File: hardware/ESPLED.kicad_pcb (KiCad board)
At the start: 2 copper layers, 100 x 50 mm, 52 parts, among them CON1 BARREL_JACK, J1 USB, J2 LED_CON_RGB, J3 LED_CON_WW, J4 MIC, P1 LED_CON_SCREW, P2 LED_CON_SCREW, P3 LED_CON_SCREW, Q1 IRLZ34N, Q2 IRLZ34N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

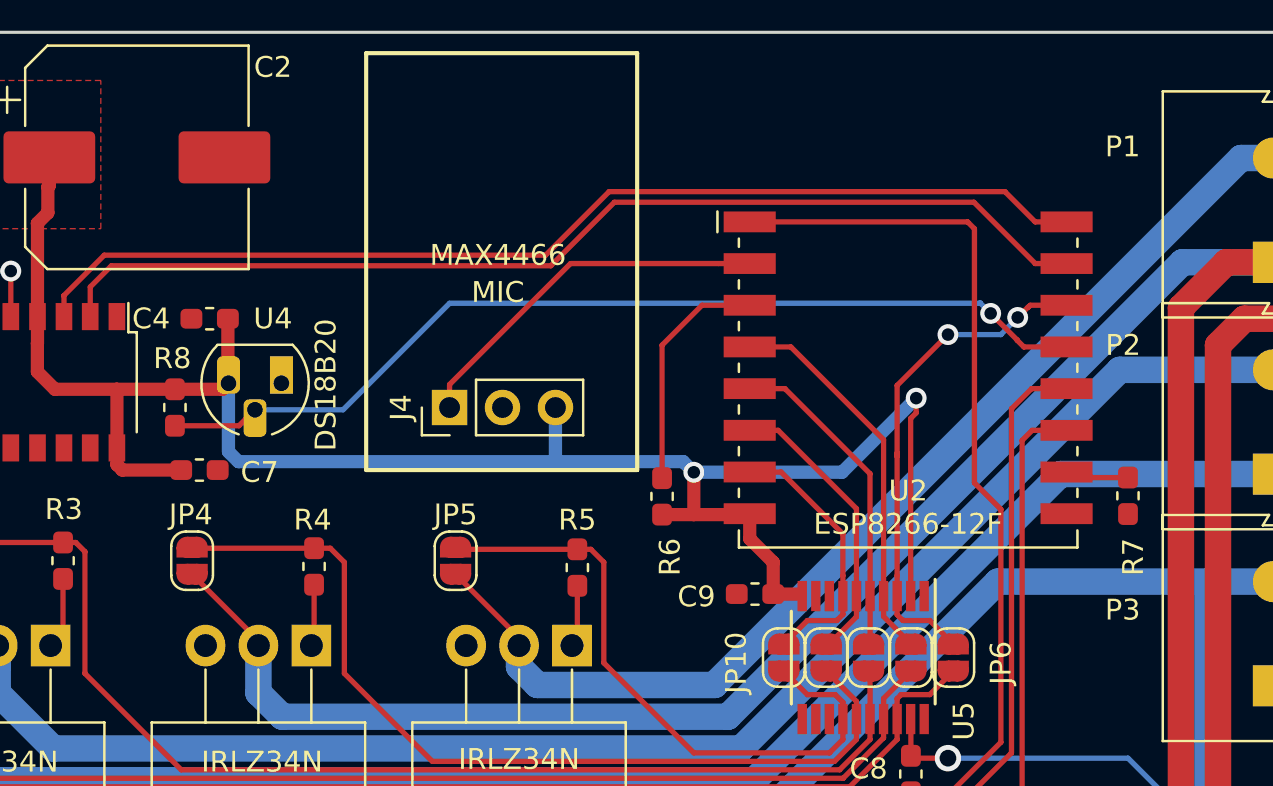
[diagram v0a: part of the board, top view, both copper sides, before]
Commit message: Change Capacitor size, fix #23 move C4 near ESP8266, fix #11 change label P1 to P3, fix #12
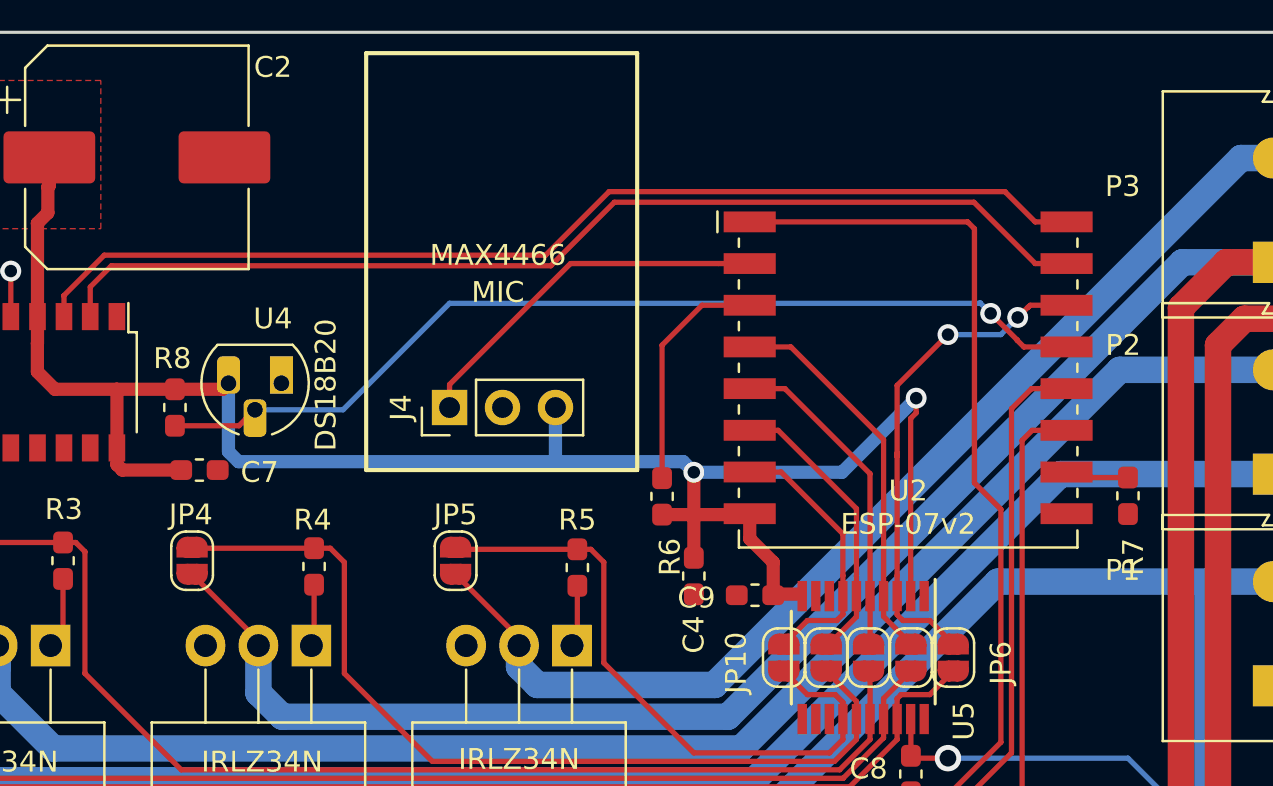
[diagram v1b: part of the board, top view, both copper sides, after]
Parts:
- C2: value 1000uF -> 22uF
- J1: value USB -> USB_B_Micro
- U2: value ESP8266-12F -> ESP-07v2
- U3: value CH340G -> INTERFACE-CH340G
- Y1: value 12MHz -> Crystal
- moved C4 26.3 mm to (156.7, 91.1), turned to 90 degrees
- moved P1 20.3 mm to (185.5, 96.4)
- moved P3 20.3 mm to (185.5, 76.0)
- moved C9 0.06 mm to (159.7, 92.0)
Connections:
- P1 pad 1: /CH4 -> +12V
- P1 pad 2: /CH5 -> /CH1
- P3 pad 1: +12V -> /CH4
- P3 pad 2: /CH1 -> /CH5
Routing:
- net +3V3: track 97.0 -> 96.0 mm
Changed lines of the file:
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@@
   (page A4)
   (layers
-    (0 F.Cu signal hide)
+    (0 F.Cu signal)
     (31 B.Cu signal hide)
     (32 B.Adhes user hide)
@@
     (44 Edge.Cuts user hide)
     (45 Margin user hide)
-    (46 B.CrtYd user hide)
-    (47 F.CrtYd user hide)
+    (46 B.CrtYd user)
+    (47 F.CrtYd user)
     (48 B.Fab user hide)
-    (49 F.Fab user hide)
+    (49 F.Fab user)
   )
   (setup
@@
     (solder_mask_min_width 0.25)
     (aux_axis_origin 0 0)
-    (visible_elements FFFFEF7F)
+    (visible_elements FFFFFF7F)
     (pcbplotparams
       (layerselection 0x00030_80000001)
@@
       (effects (font (size 1 1) (thickness 0.15)))
     )
-    (fp_text value 1000uF (at 8.43 -2.42) (layer F.Fab)
+    (fp_text value 22uF (at 8.43 -2.42) (layer F.Fab)
       (effects (font (size 1 1) (thickness 0.15)))
     )
@@
   )
   (module Capacitor_SMD:C_0603_1608Metric_Pad1.05x0.95mm_HandSolder (layer F.Cu)
-    (at 133.491 78.74)
+    (at 156.718 91.0844 90)
     (descr "Capacitor SMD 0603 (1608 Metric), square (rectangular) end terminal, IPC_7351 nominal with elongated pad for handsoldering. (Body size source: http://www.tortai-tech.com/upload/download/2011102023233369053.pdf), generated with kicad-footprint-generator")
     (tags "capacitor handsolder")
     (attr smd)
-    (fp_text reference C4 (at -2.808 0) (layer F.SilkS)
+    (fp_text reference C4 (at -2.808 0 90) (layer F.SilkS)
       (effects (font (size 1 1) (thickness 0.15)))
     )
-    (fp_text value 100nF (at 0.494 -1.27) (layer F.Fab)
+    (fp_text value 100nF (at 0.494 -1.27 90) (layer F.Fab)
       (effects (font (size 1 1) (thickness 0.15)))
     )
@@
     (fp_line (start 1.65 -0.73) (end 1.65 0.73) (layer F.CrtYd) (width 0.05))
     (fp_line (start 1.65 0.73) (end -1.65 0.73) (layer F.CrtYd) (width 0.05))
-    (fp_text user %R (at 0 0) (layer F.Fab)
+    (fp_text user %R (at 0 0 90) (layer F.Fab)
       (effects (font (size 0.4 0.4) (thickness 0.06)))
     )
-    (pad 1 smd roundrect (at -0.875 0) (size 1.05 0.95) (layers F.Cu F.Paste F.Mask) (roundrect_rratio 0.25)
+    (pad 1 smd roundrect (at -0.875 0 90) (size 1.05 0.95) (layers F.Cu F.Paste F.Mask) (roundrect_rratio 0.25)
       (net 2 GND))
-    (pad 2 smd roundrect (at 0.875 0) (size 1.05 0.95) (layers F.Cu F.Paste F.Mask) (roundrect_rratio 0.25)
+    (pad 2 smd roundrect (at 0.875 0 90) (size 1.05 0.95) (layers F.Cu F.Paste F.Mask) (roundrect_rratio 0.25)
       (net 3 +3V3))
     (model ${KISYS3DMOD}/Capacitor_SMD.3dshapes/C_0603_1608Metric.wrl
@@
       (effects (font (size 1 1) (thickness 0.15)))
     )
-    (fp_text value ESP8266-12F (at 0 9.6) (layer F.SilkS)
+    (fp_text value ESP-07v2 (at 0 9.6) (layer F.SilkS)
       (effects (font (size 1 1) (thickness 0.15)))
     )
@@
   )
   (module TerminalBlock:TerminalBlock_Altech_AK300-2_P5.00mm (layer F.Cu)
-    (at 185.515 76.032 90)
+    (at 185.515 96.352 90)
     (descr "Altech AK300 terminal block, pitch 5.0mm, 45 degree angled, see http://www.mouser.com/ds/2/16/PCBMETRC-24178.pdf")
     (tags "Altech AK300 terminal block pitch 5.0mm")
@@
     )
     (pad 2 thru_hole oval (at 5 0 90) (size 1.98 3.96) (drill 1.32) (layers *.Cu *.Mask)
-      (net 36 /CH5))
+      (net 32 /CH1))
     (pad 1 thru_hole rect (at 0 0 90) (size 1.98 3.96) (drill 1.32) (layers *.Cu *.Mask)
-      (net 35 /CH4))
+      (net 1 +12V))
     (model ${KISYS3DMOD}/TerminalBlock.3dshapes/TerminalBlock_Altech_AK300-2_P5.00mm.wrl
       (at (xyz 0 0 0))
@@
   )
   (module TerminalBlock:TerminalBlock_Altech_AK300-2_P5.00mm (layer F.Cu)
-    (at 185.515 96.352 90)
+    (at 185.515 76.032 90)
     (descr "Altech AK300 terminal block, pitch 5.0mm, 45 degree angled, see http://www.mouser.com/ds/2/16/PCBMETRC-24178.pdf")
     (tags "Altech AK300 terminal block pitch 5.0mm")
@@
     (fp_arc (start -1.13 -4.65) (end -1.42 -4.13) (angle 104.2) (layer F.Fab) (width 0.1))
     (pad 1 thru_hole rect (at 0 0 90) (size 1.98 3.96) (drill 1.32) (layers *.Cu *.Mask)
-      (net 1 +12V))
+      (net 35 /CH4))
     (pad 2 thru_hole oval (at 5 0 90) (size 1.98 3.96) (drill 1.32) (layers *.Cu *.Mask)
-      (net 32 /CH1))
+      (net 36 /CH5))
     (model ${KISYS3DMOD}/TerminalBlock.3dshapes/TerminalBlock_Altech_AK300-2_P5.00mm.wrl
       (at (xyz 0 0 0))
@@
       (effects (font (size 1 1) (thickness 0.15)))
     )
-    (fp_text value USB (at -5.08 -0.508) (layer F.Fab)
+    (fp_text value USB_B_Micro (at -5.08 -0.508) (layer F.Fab)
       (effects (font (size 1 1) (thickness 0.15)))
     )
@@
       (effects (font (size 1 1) (thickness 0.15)))
     )
-    (fp_text value 12MHz (at -9.2795 0.635 90) (layer F.Fab)
+    (fp_text value Crystal (at -9.2795 0.635 90) (layer F.Fab)
       (effects (font (size 1 1) (thickness 0.15)))
     )
@@
   )
   (module Capacitor_SMD:C_0603_1608Metric_Pad1.05x0.95mm_HandSolder (layer F.Cu)
-    (at 159.653 91.948)
+    (at 159.653 92.0044)
     (descr "Capacitor SMD 0603 (1608 Metric), square (rectangular) end terminal, IPC_7351 nominal with elongated pad for handsoldering. (Body size source: http://www.tortai-tech.com/upload/download/2011102023233369053.pdf), generated with kicad-footprint-generator")
     (tags "capacitor handsolder")
@@
       (effects (font (size 1 1) (thickness 0.15)))
     )
-    (fp_text value CH340G (at -4.953 2.671792) (layer F.Fab)
+    (fp_text value INTERFACE-CH340G (at -4.953 2.671792) (layer F.Fab)
       (effects (font (size 1 1) (thickness 0.15)))
     )
@@
   (segment (start 134.3935 81.838) (end 134.1065 82.125) (width 0.635) (layer F.Cu) (net 3) (status 30))
   (segment (start 134.366 81.8105) (end 134.3935 81.838) (width 0.635) (layer F.Cu) (net 3) (status 30))
-  (segment (start 134.366 78.74) (end 134.366 81.8105) (width 0.635) (layer F.Cu) (net 3) (status 30))
   (segment (start 134.3935 81.838) (end 134.3935 85.1175) (width 0.635) (layer B.Cu) (net 3) (status 10))
   (segment (start 134.3935 85.1175) (end 134.874 85.598) (width 0.635) (layer B.Cu) (net 3))
@@
   (segment (start 167.121 83.522106) (end 167.121 91.067) (width 0.254) (layer F.Cu) (net 3))
   (segment (start 167.386 82.55) (end 167.386 83.257106) (width 0.254) (layer F.Cu) (net 3))
+  (segment (start 156.718 90.2094) (end 156.718 88.138) (width 0.635) (layer F.Cu) (net 3))
   (segment (start 122.682 78.631413) (end 122.686792 78.636205) (width 0.254) (layer F.Cu) (net 4) (status 30))
   (segment (start 116.332 69.088) (end 122.682 75.438) (width 0.254) (layer B.Cu) (net 4))

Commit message: * Remove Temp Sensor * Redo Power Part -> Replace AMS1117 with LM2596 StepDown IC + Peripherals * Redo PCB * Replace Wrong Screw Terminal * Add aditional C10 close to OE of U5
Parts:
- removed C3: 1uF, Capacitor_SMD:C_0603_1608Metric_Pad1.05x0.95mm_HandSolder
- removed P1, P2, P3: LED_CON_SCREW, TerminalBlock:TerminalBlock_Altech_AK300-2_P5.00mm
- removed R8: 4.7K, Resistor_SMD:R_0603_1608Metric_Pad1.05x0.95mm_HandSolder
- removed U4: DS18B20, Package_TO_SOT_THT:TO-92_HandSolder
- added C10: 100nF, Capacitor_SMD:C_0603_1608Metric_Pad1.08x0.95mm_HandSolder, F.Cu at (169.7, 91.7)
- added D2: 1N5825, Diode_SMD:D_SMC_Handsoldering, F.Cu at (127.8, 84.3)
- added J5: Conn_01x06, TerminalBlock:TerminalBlock_bornier-6_P5.08mm, F.Cu at (187.7, 70.4)
- added L1: 33uH, Inductor_SMD:L_12x12mm_H8mm, F.Cu at (127.8, 74.2)
- C1: value 1uF -> 680uF; footprint Capacitor_SMD:C_0603_1608Metric_Pad1.05x0.95mm_HandSolder -> Capacitor_Tantalum_SMD:CP_EIA-6032-20_AVX-F_Pad2.25x2.35mm_HandSolder
- C2: value 22uF -> 220uF; footprint Capacitor_SMD:CP_Elec_10x10.5 -> Capacitor_Tantalum_SMD:CP_EIA-6032-20_AVX-F_Pad2.25x2.35mm_HandSolder
- C7: footprint Capacitor_SMD:C_0603_1608Metric_Pad1.05x0.95mm_HandSolder -> Capacitor_SMD:C_0603_1608Metric_Pad1.08x0.95mm_HandSolder
- U1: value AMS1117-3.3 -> LM2596T-3.3; footprint Package_TO_SOT_SMD:SOT-223-3_TabPin2 -> Package_TO_SOT_SMD:TO-263-5_TabPin3
- moved C6 28.4 mm to (140.7, 79.5)
- moved C5 24.3 mm to (137.2, 79.5), turned to 0 degrees
- moved Y1 23.1 mm to (140.0, 82.5), turned to 180 degrees
- moved C2 20.4 mm to (114.8, 84.6), turned to 180 degrees
- moved C7 20.1 mm to (144.3, 69.3), turned to 90 degrees
- moved U3 17.0 mm to (139.2, 73.0), turned to 0 degrees
- moved C1 10.7 mm to (104.9, 69.3), turned to 90 degrees
- moved R6 9.10 mm to (159.0, 79.0)
- moved R7 5.90 mm to (174.0, 91.9)
- moved J4 4.94 mm to (148.8, 86.1)
- moved U1 3.56 mm to (114.8, 74.2), turned to 90 degrees
- moved C4 2.99 mm to (159.0, 89.2)
- moved U2 2.42 mm to (169.4, 79.0)
- moved D1 2.37 mm to (103.6, 75.0)
- moved F1 1.94 mm to (101.1, 70.1)
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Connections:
- U1 pad 1: GND -> +12V
- U1 pad 2: +3V3 -> Net-(D2-Pad1)
- U1 pad 3: +12V -> GND
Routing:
- net Net-(U2-Pad13): track 46.1 -> 0.00 mm, vias 1 -> 0
- net Net-(D2-Pad1): track 0.00 -> 24.1 mm
- net Net-(J1-Pad2): track 31.6 -> 53.2 mm
- net +3V3: track 96.0 -> 117.0 mm, vias 2 -> 1
- net Net-(J1-Pad3): track 31.9 -> 50.2 mm
- net GND: track 1.25 -> 12.5 mm
- net Net-(R6-Pad2): track 11.4 -> 2.82 mm
- net /CH4: track 103.6 -> 110.1 mm
- net Net-(SW1-Pad2): track 55.9 -> 49.9 mm
- net /CH1: track 125.1 -> 131.1 mm
- net RXD: track 51.6 -> 46.3 mm
- net +12V: track 203.0 -> 207.8 mm
- net Net-(R7-Pad1): track 3.06 -> 7.11 mm
- net Net-(SW3-Pad1): track 29.6 -> 32.4 mm
- net /CH5: track 97.7 -> 100.1 mm
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- removed copper zone on F.Cu, net +3V3
